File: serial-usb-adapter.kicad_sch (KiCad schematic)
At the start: 29 parts, among them J1 USB_B_Micro, J2 UART Header, J3 USB Power, U1 LPC47M192, U2 FT231XS, Y1 SG5032CAN 14.318MHz

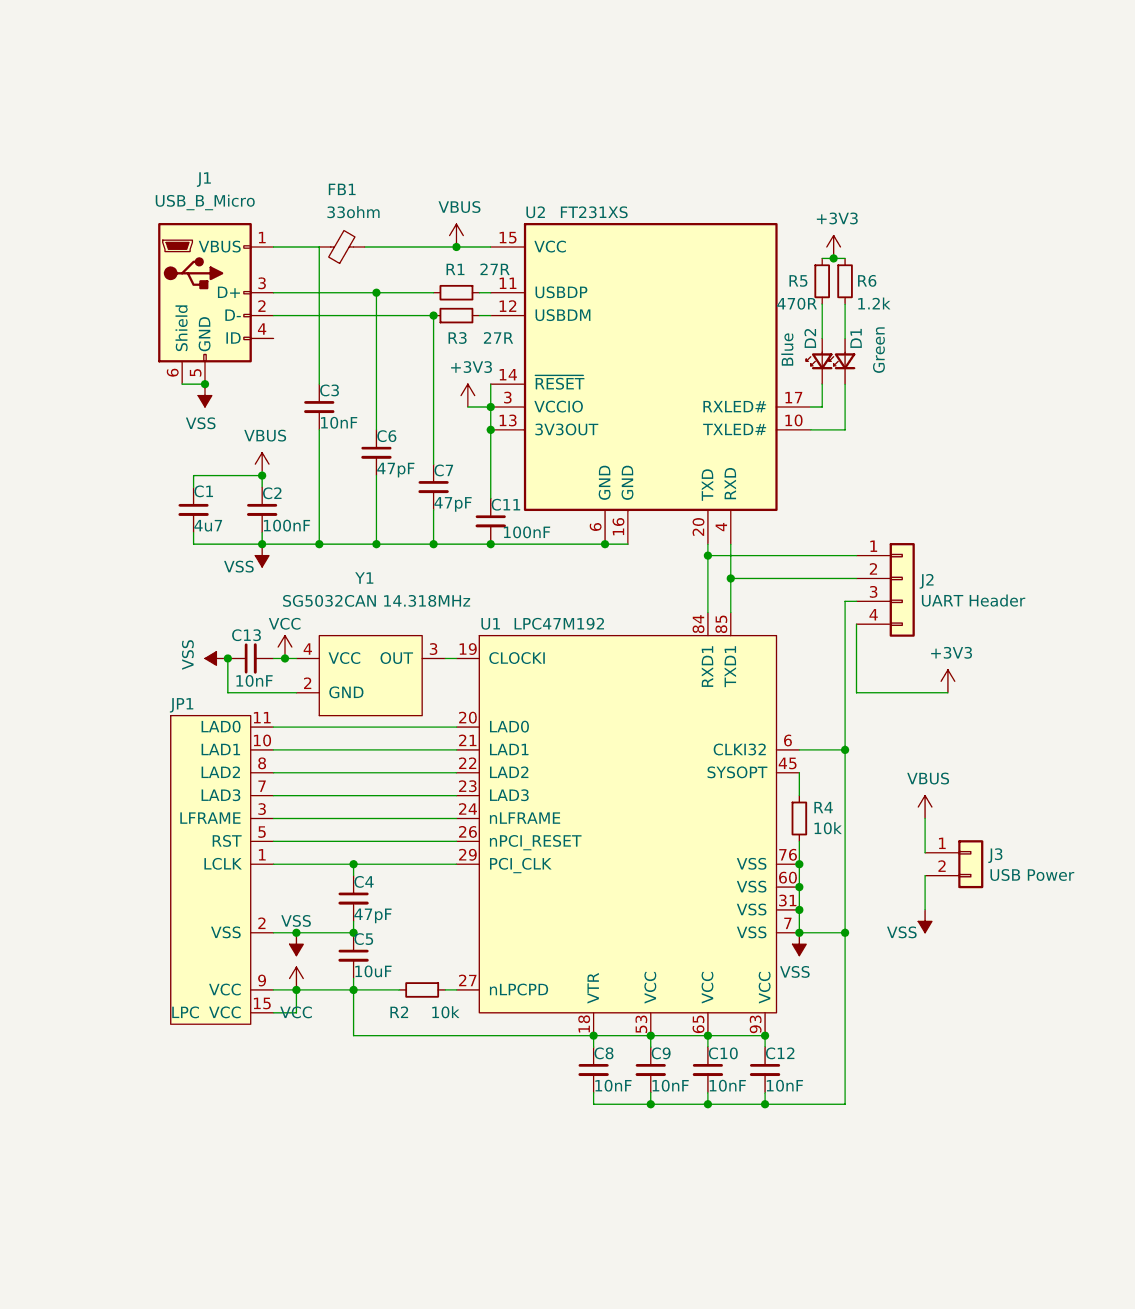
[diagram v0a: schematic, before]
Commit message: Adds USB-C based Xbox Serial USB Adapter (Rev D)
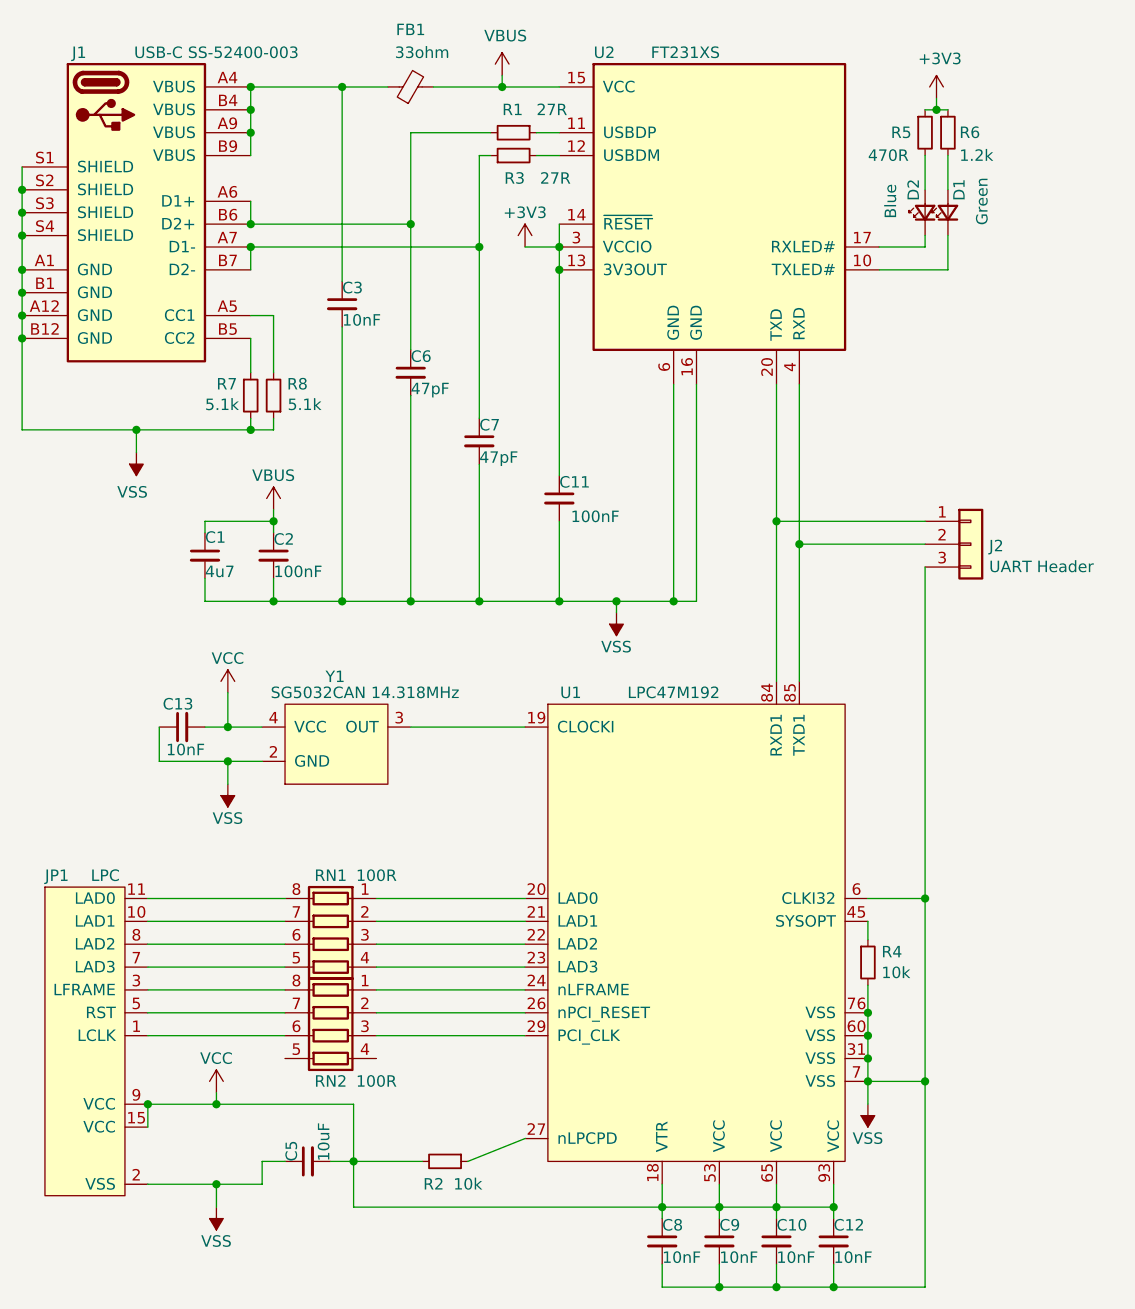
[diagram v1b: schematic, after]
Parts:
- removed C4: 47pF, Capacitor_SMD:C_0603_1608Metric, symbol Device:C_Small
- removed J1: USB_B_Micro, Connector_USB:USB_Micro-B_Wuerth_629105150521, symbol Connector:USB_B_Micro
- removed J3: USB Power, Connector_PinHeader_2.54mm:PinHeader_1x02_P2.54mm_Vertical, symbol Connector_Generic:Conn_01x02
- added J1: USB-C SS-52400-003, Library:SS-52400-003, symbol Connector:USB_C_Plug_USB2.0
- added R7, R8: 5.1k, Resistor_SMD:R_0603_1608Metric, symbol Device:R_Small
- added RN1, RN2: 100R, Resistor_SMD:R_Array_Convex_4x0603, symbol Device:R_Pack04
- C1: LCSC (none) -> C19666
- C10, C12, C13, C3, C8, C9: LCSC (none) -> C57112
- C11, C2: LCSC (none) -> C14663
- C5: LCSC (none) -> C19702
- C6, C7: LCSC (none) -> C1671
- D1: LCSC (none) -> C72043
- D2: LCSC (none) -> C72041
- FB1: LCSC (none) -> C88984
- J2: footprint Connector_PinHeader_2.54mm:PinHeader_1x04_P2.54mm_Vertical -> Connector_PinHeader_2.54mm:PinHeader_1x03_P2.54mm_Vertical; symbol Connector_Generic:Conn_01x04 -> Connector_Generic:Conn_01x03
- R1, R3: LCSC (none) -> C25190
- R2, R4: LCSC (none) -> C25804
- R5: LCSC (none) -> C23179
- R6: LCSC (none) -> C22765
- U2: LCSC (none) -> C132160
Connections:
- net +3V3: no longer J2.4 (Pin_4)
- net VSS: now also J1.A1 (GND), J1.A12 (GND), J1.B1 (GND), J1.B12 (GND), J1.S1 (SHIELD), J1.S2 (SHIELD), J1.S3 (SHIELD), J1.S4 (SHIELD), R7.2, R8.1
- net at JP1.1 (LCLK): now also RN2.6 (R3.2); no longer U1.29 (PCI_CLK)
- net at JP1.10 (LAD1): now also RN1.7 (R2.2); no longer U1.21 (LAD1)
- net at JP1.11 (LAD0): now also RN1.8 (R1.2); no longer U1.20 (LAD0)
- net at JP1.3 (LFRAME): now also RN2.8 (R1.2); no longer U1.24 (nLFRAME)
- net at JP1.5 (RST): now also RN2.7 (R2.2); no longer U1.26 (nPCI_RESET)
- net at JP1.7 (LAD3): now also RN1.5 (R4.2); no longer U1.23 (LAD3)
- net at JP1.8 (LAD2): now also RN1.6 (R3.2); no longer U1.22 (LAD2)
- net at C6.1, R1.2: now also J1.A6 (D1+), J1.B6 (D2+)
- net at C7.1, R3.1: now also J1.A7 (D1-), J1.B7 (D2-)
- net at C3.1, FB1.1: now also J1.A4 (VBUS), J1.A9 (VBUS), J1.B4 (VBUS), J1.B9 (VBUS)
- new net: RN1.1 (R1.1), U1.20 (LAD0)
- new net: RN1.2 (R2.1), U1.21 (LAD1)
- new net: RN1.3 (R3.1), U1.22 (LAD2)
- new net: RN1.4 (R4.1), U1.23 (LAD3)
- new net: RN2.1 (R1.1), U1.24 (nLFRAME)
- new net: RN2.2 (R2.1), U1.26 (nPCI_RESET)
- new net: RN2.3 (R3.1), U1.29 (PCI_CLK)
- new net: J1.A5 (CC1), R8.2
- new net: J1.B5 (CC2), R7.1
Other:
- moved on the sheet: C1, C10, C11, C12, C13, C2, C3, C5, C6, C7, C8, C9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
